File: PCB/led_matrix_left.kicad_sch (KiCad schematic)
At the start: 42 parts

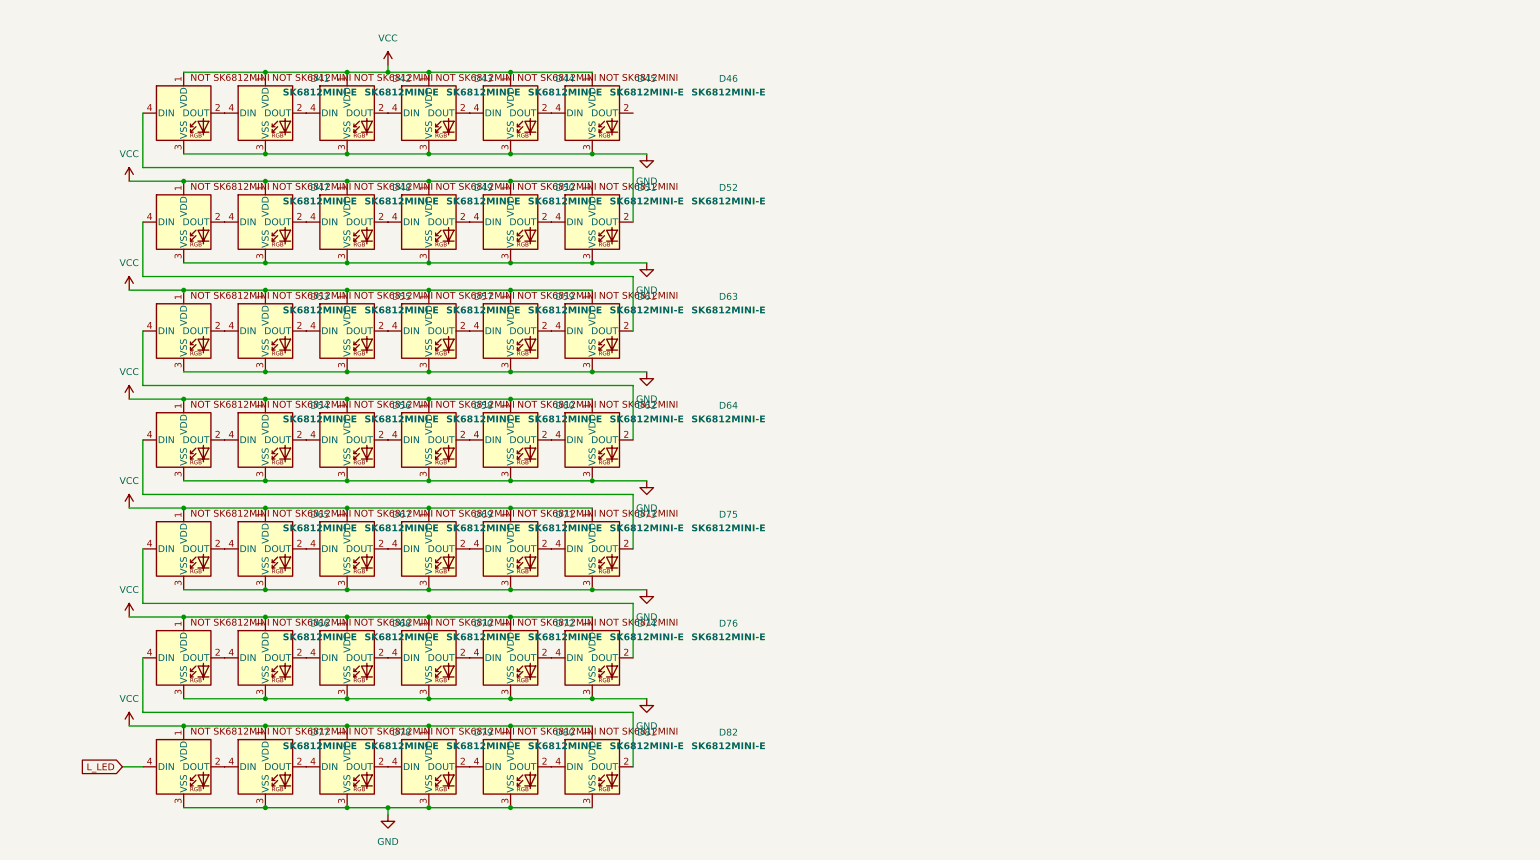
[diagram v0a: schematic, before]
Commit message: routed the switches and diodes
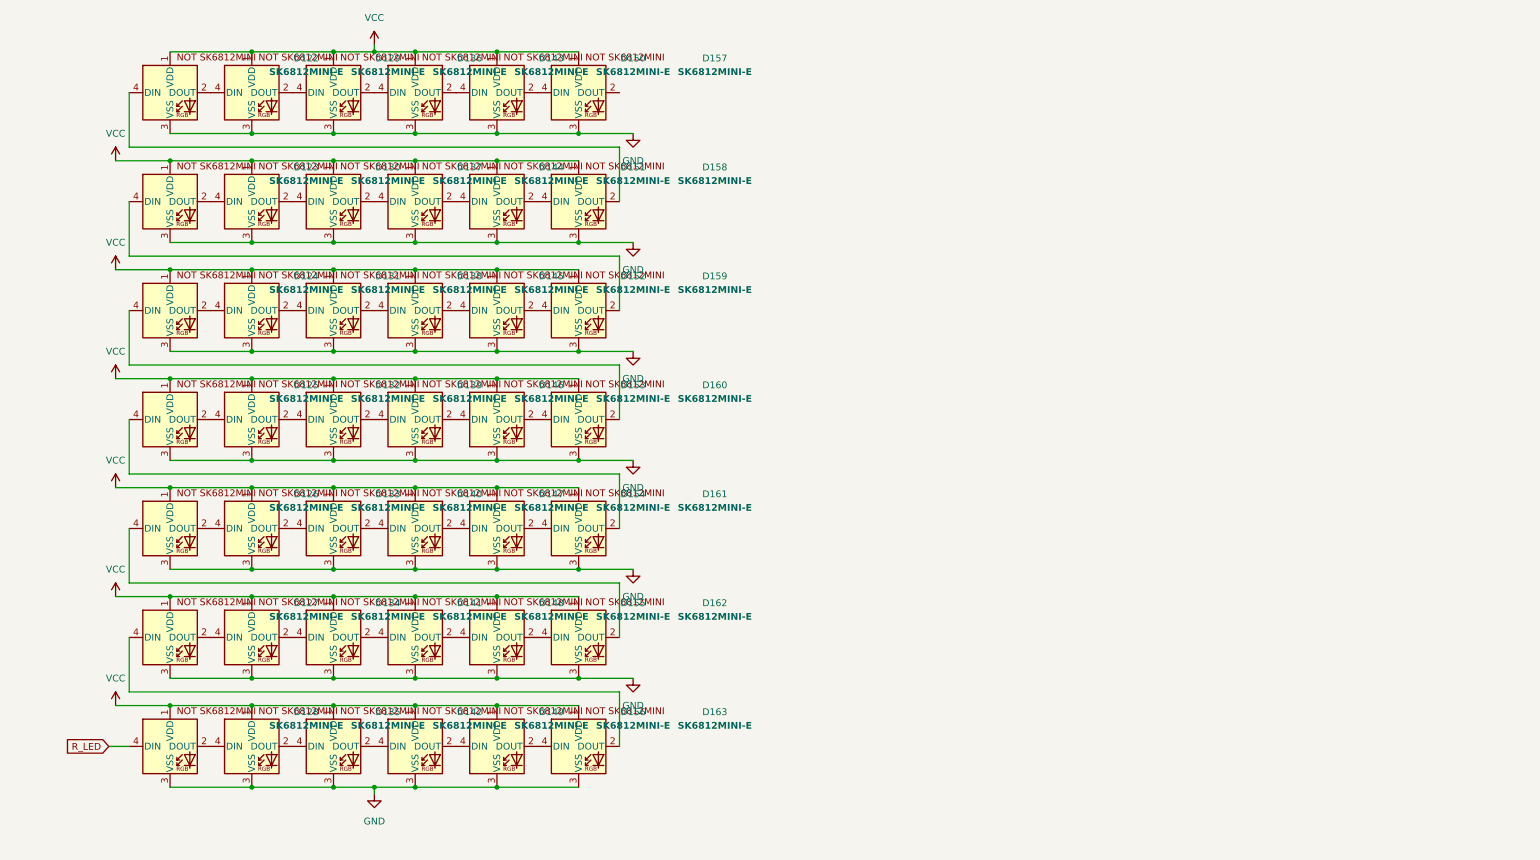
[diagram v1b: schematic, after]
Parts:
- removed D41, D42, D43, D44, D45, D46, D47, D48, D49, D50, D51, D52, D53, D54, D55, D56, D57, D58, D59, D60, D61, D62, D63, D64, D65, D66, D67, D68, D69, D70, D71, D72, D73, D74, D75, D76, D77, D78, D79, D80, D81, D82: SK6812MINI-E, footprints:SK6812MINI-E_fixed, symbol SK6812MINI-E:SK6812MINI-E
- added D122, D123, D124, D125, D126, D127, D128, D129, D130, D131, D132, D133, D134, D135, D136, D137, D138, D139, D140, D141, D142, D143, D144, D145, D146, D147, D148, D149, D150, D151, D152, D153, D154, D155, D156, D157, D158, D159, D160, D161, D162, D163: SK6812MINI-E, footprints:SK6812MINI-E_fixed, symbol SK6812MINI-E:SK6812MINI-E
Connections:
- net GND: now also D122.3 (VSS), D123.3 (VSS), D124.3 (VSS), D125.3 (VSS), D126.3 (VSS), D127.3 (VSS), D128.3 (VSS), D129.3 (VSS), D130.3 (VSS), D131.3 (VSS), D132.3 (VSS), D133.3 (VSS), D134.3 (VSS), D135.3 (VSS), D136.3 (VSS), D137.3 (VSS), D138.3 (VSS), D139.3 (VSS), D140.3 (VSS), D141.3 (VSS), D142.3 (VSS), D143.3 (VSS), D144.3 (VSS), D145.3 (VSS), D146.3 (VSS), D147.3 (VSS), D148.3 (VSS), D149.3 (VSS), D150.3 (VSS), D151.3 (VSS), D152.3 (VSS), D153.3 (VSS), D154.3 (VSS), D155.3 (VSS), D156.3 (VSS), D157.3 (VSS), D158.3 (VSS), D159.3 (VSS), D160.3 (VSS), D161.3 (VSS), D162.3 (VSS), D163.3 (VSS)
- net VCC: now also D122.1 (VDD), D123.1 (VDD), D124.1 (VDD), D125.1 (VDD), D126.1 (VDD), D127.1 (VDD), D128.1 (VDD), D129.1 (VDD), D130.1 (VDD), D131.1 (VDD), D132.1 (VDD), D133.1 (VDD), D134.1 (VDD), D135.1 (VDD), D136.1 (VDD), D137.1 (VDD), D138.1 (VDD), D139.1 (VDD), D140.1 (VDD), D141.1 (VDD), D142.1 (VDD), D143.1 (VDD), D144.1 (VDD), D145.1 (VDD), D146.1 (VDD), D147.1 (VDD), D148.1 (VDD), D149.1 (VDD), D150.1 (VDD), D151.1 (VDD), D152.1 (VDD), D153.1 (VDD), D154.1 (VDD), D155.1 (VDD), D156.1 (VDD), D157.1 (VDD), D158.1 (VDD), D159.1 (VDD), D160.1 (VDD), D161.1 (VDD), D162.1 (VDD), D163.1 (VDD)
- new net: D123.4 (DIN), D159.2 (DOUT)
- new net: D152.2 (DOUT), D159.4 (DIN)
- new net: D134.2 (DOUT), D141.4 (DIN)
- new net: D127.2 (DOUT), D134.4 (DIN)
- new net: D151.2 (DOUT), D158.4 (DIN)
- new net: D144.2 (DOUT), D151.4 (DIN)
- new net: D122.2 (DOUT), D129.4 (DIN)
- new net: D122.4 (DIN), D158.2 (DOUT)
- new net: D155.2 (DOUT), D162.4 (DIN)
- new net: D148.2 (DOUT), D155.4 (DIN)
- new net: D132.2 (DOUT), D139.4 (DIN)
- new net: D125.2 (DOUT), D132.4 (DIN)
- new net: D141.2 (DOUT), D148.4 (DIN)
- new net: D131.2 (DOUT), D138.4 (DIN)
- new net: D124.2 (DOUT), D131.4 (DIN)
- new net: D124.4 (DIN), D160.2 (DOUT)
- new net: D139.2 (DOUT), D146.4 (DIN)
- new net: D126.2 (DOUT), D133.4 (DIN)
- new net: D126.4 (DIN), D162.2 (DOUT)
- new net: D137.2 (DOUT), D144.4 (DIN)
- new net: D127.4 (DIN), D163.2 (DOUT)
- new net: D125.4 (DIN), D161.2 (DOUT)
- new net: D154.2 (DOUT), D161.4 (DIN)
- new net: D130.2 (DOUT), D137.4 (DIN)
- new net: D123.2 (DOUT), D130.4 (DIN)
- new net: D153.2 (DOUT), D160.4 (DIN)
- new net: D146.2 (DOUT), D153.4 (DIN)
- new net: D156.2 (DOUT), D163.4 (DIN)
- new net: D149.2 (DOUT), D156.4 (DIN)
- new net: D145.2 (DOUT), D152.4 (DIN)
- new net: D128.2 (DOUT), D135.4 (DIN)
- new net: D147.2 (DOUT), D154.4 (DIN)
- new net: D140.2 (DOUT), D147.4 (DIN)
- new net: D129.2 (DOUT), D136.4 (DIN)
- new net: D142.2 (DOUT), D149.4 (DIN)
- new net: D138.2 (DOUT), D145.4 (DIN)
- new net: D136.2 (DOUT), D143.4 (DIN)
- new net: D133.2 (DOUT), D140.4 (DIN)
- new net: D135.2 (DOUT), D142.4 (DIN)
- new net: D150.2 (DOUT), D157.4 (DIN)
- new net: D143.2 (DOUT), D150.4 (DIN)
- new net R_LED: D128.4 (DIN)

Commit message: redid the leds
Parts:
- removed D156, D157, D158, D159, D160, D161, D162, D163: SK6812MINI-E, footprints:SK6812MINI-E_fixed, symbol SK6812MINI-E:SK6812MINI-E
- added D79, D80, D81, D82: SK6812MINI-E, SK6812MINI-E - 3.2x2.8x1.78mm, symbol SK6812MINI-E:SK6812MINI-E
- D122, D123, D124, D125, D126, D127, D128, D129, D130, D131, D132, D133, D134, D135, D136, D137, D138, D139, D140, D141, D142, D143, D144, D145, D146, D147, D148, D149, D150, D151, D152, D153, D154, D155: footprint footprints:SK6812MINI-E_fixed -> SK6812MINI-E - 3.2x2.8x1.78mm
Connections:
- net R_LED is gone; now on an unnamed net: D128.4 (DIN)
- net GND: now also D79.3 (VSS), D80.3 (VSS), D81.3 (VSS), D82.3 (VSS)
- net VCC: now also D79.1 (VDD), D80.1 (VDD), D81.1 (VDD), D82.1 (VDD)
- net at D123.4 (DIN): now also D122.2 (DOUT)
- net at D152.2 (DOUT): now also D153.4 (DIN)
- net at D134.2 (DOUT): now also D135.4 (DIN); no longer D141.4 (DIN)
- net at D127.2 (DOUT): no longer D134.4 (DIN)
- net at D151.2 (DOUT): now also D152.4 (DIN)
- net at D144.2 (DOUT): now also D145.4 (DIN); no longer D151.4 (DIN)
- net at D129.4 (DIN): now also D128.2 (DOUT); no longer D122.2 (DOUT)
- net at D122.4 (DIN): now also D82.2 (DOUT)
- net at D155.4 (DIN): now also D154.2 (DOUT); no longer D148.2 (DOUT)
- net at D139.4 (DIN): now also D138.2 (DOUT); no longer D132.2 (DOUT)
- net at D132.4 (DIN): now also D131.2 (DOUT); no longer D125.2 (DOUT)
- net at D141.2 (DOUT): now also D142.4 (DIN); no longer D148.4 (DIN)
- net at D138.4 (DIN): now also D137.2 (DOUT); no longer D131.2 (DOUT)
- net at D131.4 (DIN): now also D130.2 (DOUT); no longer D124.2 (DOUT)
- net at D124.4 (DIN): now also D123.2 (DOUT)
- net at D146.4 (DIN): now also D145.2 (DOUT); no longer D139.2 (DOUT)
- net at D126.2 (DOUT): now also D127.4 (DIN); no longer D133.4 (DIN)
- net at D126.4 (DIN): now also D125.2 (DOUT)
- net at D144.4 (DIN): now also D143.2 (DOUT); no longer D137.2 (DOUT)
- net at D125.4 (DIN): now also D124.2 (DOUT)
- net at D137.4 (DIN): now also D136.2 (DOUT); no longer D130.2 (DOUT)
- net at D130.4 (DIN): now also D129.2 (DOUT); no longer D123.2 (DOUT)
- net at D153.2 (DOUT): now also D154.4 (DIN)
- net at D146.2 (DOUT): now also D147.4 (DIN); no longer D153.4 (DIN)
- net at D149.2 (DOUT): now also D150.4 (DIN)
- net at D147.2 (DOUT): now also D148.4 (DIN); no longer D154.4 (DIN)
- net at D140.2 (DOUT): now also D141.4 (DIN); no longer D147.4 (DIN)
- net at D136.4 (DIN): now also D135.2 (DOUT); no longer D129.2 (DOUT)
- net at D142.2 (DOUT): now also D143.4 (DIN); no longer D149.4 (DIN)
- net at D133.2 (DOUT): now also D134.4 (DIN); no longer D140.4 (DIN)
- net at D150.2 (DOUT): now also D151.4 (DIN)
- new net: D79.2 (DOUT), D80.4 (DIN)
- new net: D81.2 (DOUT), D82.4 (DIN)
- new net: D80.2 (DOUT), D81.4 (DIN)
- new net: D132.2 (DOUT), D133.4 (DIN)
- new net: D148.2 (DOUT), D149.4 (DIN)
- new net: D139.2 (DOUT), D140.4 (DIN)
- new net L_LED: D79.4 (DIN)
- no-connect marks 0 -> 1

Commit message: "finished" right side
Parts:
- added D157: SK6812MINI-E, footprints:SK6812MINI-E_fixed, symbol SK6812MINI-E:SK6812MINI-E
- D122, D123, D124, D125, D126, D127, D128, D129, D130, D131, D132, D133, D134, D135, D136, D137, D138, D139, D140, D141, D142, D143, D144, D145, D146, D147, D148, D149, D150, D151, D152, D153, D154, D155, D79, D80, D81, D82: footprint SK6812MINI-E - 3.2x2.8x1.78mm -> footprints:SK6812MINI-E_fixed
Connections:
- net GND: now also D157.3 (VSS)
- net VCC: now also D157.1 (VDD)
- net at D155.2 (DOUT): now also D157.4 (DIN)
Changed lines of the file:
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@@
 	)
 	(junction
+		(at 110.49 63.5)
+		(diameter 0)
+		(color 0 0 0 0)
+	)
+	(junction
 		(at 232.41 55.88)
 		(diameter 0)
@@
 	)
 	(junction
+		(at 110.49 78.74)
+		(diameter 0)
+		(color 0 0 0 0)
+	)
+	(junction
 		(at 49.53 55.88)
 		(diameter 0)
@@
 	)
 	(junction
-		(at 110.49 63.5)
-		(diameter 0)
-		(color 0 0 0 0)
-	)
-	(junction
 		(at 125.73 55.88)
 		(diameter 0)
@@
 	)
 	(junction
+		(at 125.73 63.5)
+		(diameter 0)
+		(color 0 0 0 0)
+	)
+	(junction
 		(at 64.77 63.5)
 		(diameter 0)
@@
 	)
 	(no_connect
-		(at 118.11 71.12)
+		(at 133.35 71.12)
 	)
 	(wire
@@
 	(wire
 		(pts
-			(xy 273.05 63.5) (xy 110.49 63.5)
+			(xy 125.73 17.78) (xy 140.97 17.78)
 		)
 		(stroke
@@
 	(wire
 		(pts
-			(xy 125.73 17.78) (xy 140.97 17.78)
+			(xy 110.49 78.74) (xy 125.73 78.74)
 		)
 		(stroke
@@
 	(wire
 		(pts
+			(xy 125.73 63.5) (xy 273.05 63.5)
+		)
+		(stroke
+			(width 0)
+			(type default)
+		)
+	)
+	(wire
+		(pts
 			(xy 217.17 33.02) (xy 232.41 33.02)
 		)
@@
 	(wire
 		(pts
+			(xy 110.49 63.5) (xy 125.73 63.5)
+		)
+		(stroke
+			(width 0)
+			(type default)
+		)
+	)
+	(wire
+		(pts
 			(xy 232.41 17.78) (xy 247.65 17.78)
 		)
@@
 			)
 		)
-		(property "Footprint" "SK6812MINI-E - 3.2x2.8x1.78mm"
+		(property "Footprint" "footprints:SK6812MINI-E_fixed"
 			(at 66.04 78.74 0)
 			(effects
@@
 			)
 		)
-		(property "Footprint" "SK6812MINI-E - 3.2x2.8x1.78mm"
+		(property "Footprint" "footprints:SK6812MINI-E_fixed"
 			(at 35.56 33.02 0)
 			(effects
@@
 			)
 		)
-		(property "Footprint" "SK6812MINI-E - 3.2x2.8x1.78mm"
+		(property "Footprint" "footprints:SK6812MINI-E_fixed"
 			(at 66.04 33.02 0)
 			(effects
@@
 			)
 		)
-		(property "Footprint" "SK6812MINI-E - 3.2x2.8x1.78mm"
+		(property "Footprint" "footprints:SK6812MINI-E_fixed"
 			(at 187.96 55.88 0)
 			(effects
@@
 			)
 		)
-		(property "Footprint" "SK6812MINI-E - 3.2x2.8x1.78mm"
+		(property "Footprint" "footprints:SK6812MINI-E_fixed"
 			(at 172.72 55.88 0)
 			(effects
@@
 			)
 		)
-		(property "Footprint" "SK6812MINI-E - 3.2x2.8x1.78mm"
+		(property "Footprint" "footprints:SK6812MINI-E_fixed"
 			(at 187.96 33.02 0)
 			(effects
@@
 			)
 		)
-		(property "Footprint" "SK6812MINI-E - 3.2x2.8x1.78mm"
+		(property "Footprint" "footprints:SK6812MINI-E_fixed"
 			(at 172.72 33.02 0)
 			(effects
@@
 			)
 		)
-		(property "Footprint" "SK6812MINI-E - 3.2x2.8x1.78mm"
+		(property "Footprint" "footprints:SK6812MINI-E_fixed"
 			(at 218.44 33.02 0)
 			(effects
@@
 			)
 		)
-		(property "Footprint" "SK6812MINI-E - 3.2x2.8x1.78mm"
+		(property "Footprint" "footprints:SK6812MINI-E_fixed"
 			(at 157.48 55.88 0)
 			(effects
@@
 			)
 		)
-		(property "Footprint" "SK6812MINI-E - 3.2x2.8x1.78mm"
+		(property "Footprint" "footprints:SK6812MINI-E_fixed"
 			(at 111.76 33.02 0)
 			(effects
@@
 			)
 		)
-		(property "Footprint" "SK6812MINI-E - 3.2x2.8x1.78mm"
+		(property "Footprint" "footprints:SK6812MINI-E_fixed"
 			(at 50.8 55.88 0)
 			(effects
@@
 			)
 		)
-		(property "Footprint" "SK6812MINI-E - 3.2x2.8x1.78mm"
+		(property "Footprint" "footprints:SK6812MINI-E_fixed"
 			(at 233.68 33.02 0)
 			(effects
@@
 			)
 		)
-		(property "Footprint" "SK6812MINI-E - 3.2x2.8x1.78mm"
+		(property "Footprint" "footprints:SK6812MINI-E_fixed"
 			(at 50.8 78.74 0)
 			(effects
@@
 			)
 		)
-		(property "Footprint" "SK6812MINI-E - 3.2x2.8x1.78mm"
+		(property "Footprint" "footprints:SK6812MINI-E_fixed"
 			(at 96.52 55.88 0)
 			(effects
@@
 			)
 		)
-		(property "Footprint" "SK6812MINI-E - 3.2x2.8x1.78mm"
+		(property "Footprint" "footprints:SK6812MINI-E_fixed"
 			(at 127 33.02 0)
 			(effects
@@
 			)
 		)
-		(property "Footprint" "SK6812MINI-E - 3.2x2.8x1.78mm"
+		(property "Footprint" "footprints:SK6812MINI-E_fixed"
 			(at 66.04 55.88 0)
 			(effects
@@
 			)
 		)
-		(property "Footprint" "SK6812MINI-E - 3.2x2.8x1.78mm"
+		(property "Footprint" "footprints:SK6812MINI-E_fixed"
 			(at 96.52 78.74 0)
 			(effects
@@
 			)
 		)
-		(property "Footprint" "SK6812MINI-E - 3.2x2.8x1.78mm"
+		(property "Footprint" "footprints:SK6812MINI-E_fixed"
 			(at 35.56 55.88 0)
 			(effects
@@
 			)
 		)
-		(property "Footprint" "SK6812MINI-E - 3.2x2.8x1.78mm"
+		(property "Footprint" "footprints:SK6812MINI-E_fixed"
 			(at 203.2 55.88 0)
 			(effects
@@
 	(symbol
 		(lib_id "SK6812MINI-E:SK6812MINI-E")
+		(at 125.73 71.12 0)
+		(unit 1)
+		(exclude_from_sim no)
+		(in_bom yes)
+		(on_board yes)
+		(dnp no)
+		(fields_autoplaced yes)
+		(property "Reference" "D157"
+			(at 151.13 64.6998 0)
+			(effects
+				(font
+					(size 1.27 1.27)
+				)
+			)
+		)
+		(property "Value" "SK6812MINI-E"
+			(at 151.13 67.2399 0)
+			(effects
+				(font
+					(size 1.27 1.27)
+					(thickness 0.254)
+					(bold yes)
+				)
+			)
+		)
+		(property "Footprint" "footprints:SK6812MINI-E_fixed"
+			(at 127 78.74 0)
+			(effects
+				(font
+					(size 1.27 1.27)
+				)
+				(justify left top)
+				(hide yes)
+			)
+		)
+		(property "Datasheet" "https://cdn-shop.adafruit.com/product-files/4960/4960_SK6812MINI-E_REV02_EN.pdf"
+			(at 128.27 80.645 0)
+			(effects
+				(font
+					(size 1.27 1.27)
+				)
+				(justify left top)
+				(hide yes)
+			)
+		)
+		(property "Description" "RGB LED with integrated controller"
+			(at 125.73 71.12 0)
+			(effects
+				(font
+					(size 1.27 1.27)
+				)
+				(hide yes)
+			)
+		)
+		(pin "3"
+		)
+		(pin "4"
+		)
+		(pin "2"
+		)
+		(pin "1"
+		)
+		(instances
+			(project "split_keeb"
+				(path "/b7eb43b0-c363-4b01-b49e-ca46ab5210f5/ae4bea95-4bbe-46f1-a2e1-77f68a6f565b/778f6772-18fc-4b17-be33-62b3fac16c33"
+					(reference "D157")
+					(unit 1)
+				)
+			)
+		)
+	)
+	(symbol
+		(lib_id "SK6812MINI-E:SK6812MINI-E")
 		(at 262.89 25.4 0)
 		(unit 1)
@@
 			)
 		)
-		(property "Footprint" "SK6812MINI-E - 3.2x2.8x1.78mm"
+		(property "Footprint" "footprints:SK6812MINI-E_fixed"
 			(at 264.16 33.02 0)
 			(effects
@@
 			)
 		)
-		(property "Footprint" "SK6812MINI-E - 3.2x2.8x1.78mm"
+		(property "Footprint" "footprints:SK6812MINI-E_fixed"
 			(at 81.28 55.88 0)
 			(effects
@@
 			)
 		)
-		(property "Footprint" "SK6812MINI-E - 3.2x2.8x1.78mm"
+		(property "Footprint" "footprints:SK6812MINI-E_fixed"
 			(at 142.24 55.88 0)
 			(effects
@@
 			)
 		)
-		(property "Footprint" "SK6812MINI-E - 3.2x2.8x1.78mm"
+		(property "Footprint" "footprints:SK6812MINI-E_fixed"
 			(at 142.24 33.02 0)
 			(effects
@@
 			)
 		)
-		(property "Footprint" "SK6812MINI-E - 3.2x2.8x1.78mm"
+		(property "Footprint" "footprints:SK6812MINI-E_fixed"
 			(at 50.8 33.02 0)
 			(effects
@@
 			)
 		)
-		(property "Footprint" "SK6812MINI-E - 3.2x2.8x1.78mm"
+		(property "Footprint" "footprints:SK6812MINI-E_fixed"
 			(at 35.56 78.74 0)
 			(effects
@@
 			)
 		)
-		(property "Footprint" "SK6812MINI-E - 3.2x2.8x1.78mm"
+		(property "Footprint" "footprints:SK6812MINI-E_fixed"
 			(at 248.92 55.88 0)
 			(effects
@@
 			)
 		)
-		(property "Footprint" "SK6812MINI-E - 3.2x2.8x1.78mm"
+		(property "Footprint" "footprints:SK6812MINI-E_fixed"
 			(at 111.76 78.74 0)
 			(effects
@@
 			)
 		)
-		(property "Footprint" "SK6812MINI-E - 3.2x2.8x1.78mm"
+		(property "Footprint" "footprints:SK6812MINI-E_fixed"
 			(at 218.44 55.88 0)
 			(effects
@@
 			)
 		)
-		(property "Footprint" "SK6812MINI-E - 3.2x2.8x1.78mm"
+		(property "Footprint" "footprints:SK6812MINI-E_fixed"
 			(at 127 55.88 0)
 			(effects
@@
 			)
 		)
-		(property "Footprint" "SK6812MINI-E - 3.2x2.8x1.78mm"
+		(property "Footprint" "footprints:SK6812MINI-E_fixed"
 			(at 264.16 55.88 0)
 			(effects
@@
 			)
 		)
-		(property "Footprint" "SK6812MINI-E - 3.2x2.8x1.78mm"
+		(property "Footprint" "footprints:SK6812MINI-E_fixed"
 			(at 233.68 55.88 0)
 			(effects
@@
 			)
 		)
-		(property "Footprint" "SK6812MINI-E - 3.2x2.8x1.78mm"
+		(property "Footprint" "footprints:SK6812MINI-E_fixed"
 			(at 248.92 33.02 0)
 			(effects
@@
 			)
 		)
-		(property "Footprint" "SK6812MINI-E - 3.2x2.8x1.78mm"
+		(property "Footprint" "footprints:SK6812MINI-E_fixed"
 			(at 81.28 78.74 0)
 			(effects
@@
 			)
 		)
-		(property "Footprint" "SK6812MINI-E - 3.2x2.8x1.78mm"
+		(property "Footprint" "footprints:SK6812MINI-E_fixed"
 			(at 157.48 33.02 0)
 			(effects
@@
 			)
 		)
-		(property "Footprint" "SK6812MINI-E - 3.2x2.8x1.78mm"
+		(property "Footprint" "footprints:SK6812MINI-E_fixed"
 			(at 96.52 33.02 0)
 			(effects
@@
 			)
 		)
-		(property "Footprint" "SK6812MINI-E - 3.2x2.8x1.78mm"
+		(property "Footprint" "footprints:SK6812MINI-E_fixed"
 			(at 111.76 55.88 0)
 			(effects
@@
 			)
 		)
-		(property "Footprint" "SK6812MINI-E - 3.2x2.8x1.78mm"
+		(property "Footprint" "footprints:SK6812MINI-E_fixed"
 			(at 203.2 33.02 0)
 			(effects
@@
 			)
 		)
-		(property "Footprint" "SK6812MINI-E - 3.2x2.8x1.78mm"
+		(property "Footprint" "footprints:SK6812MINI-E_fixed"
 			(at 81.28 33.02 0)
 			(effects
